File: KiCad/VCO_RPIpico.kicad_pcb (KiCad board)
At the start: 2 copper layers, 142 x 89 mm, 91 parts, among them J1 AudioJack2, J2 Power Jack, SW1 LFO1/2, SW2 Select LFO WaveForm, SW3 Fire4, SW4 Fire3, SW5 Fire2, SW6 Fire1, SW7 Shift2/Save, SW8 Shift1 / Select Bank, U2 PT2399, U3 L7805, sw10 sw_led_fire2, sw11 sw_led_fire3, sw12 sw_led_fire4, sw9 sw_led_fire1

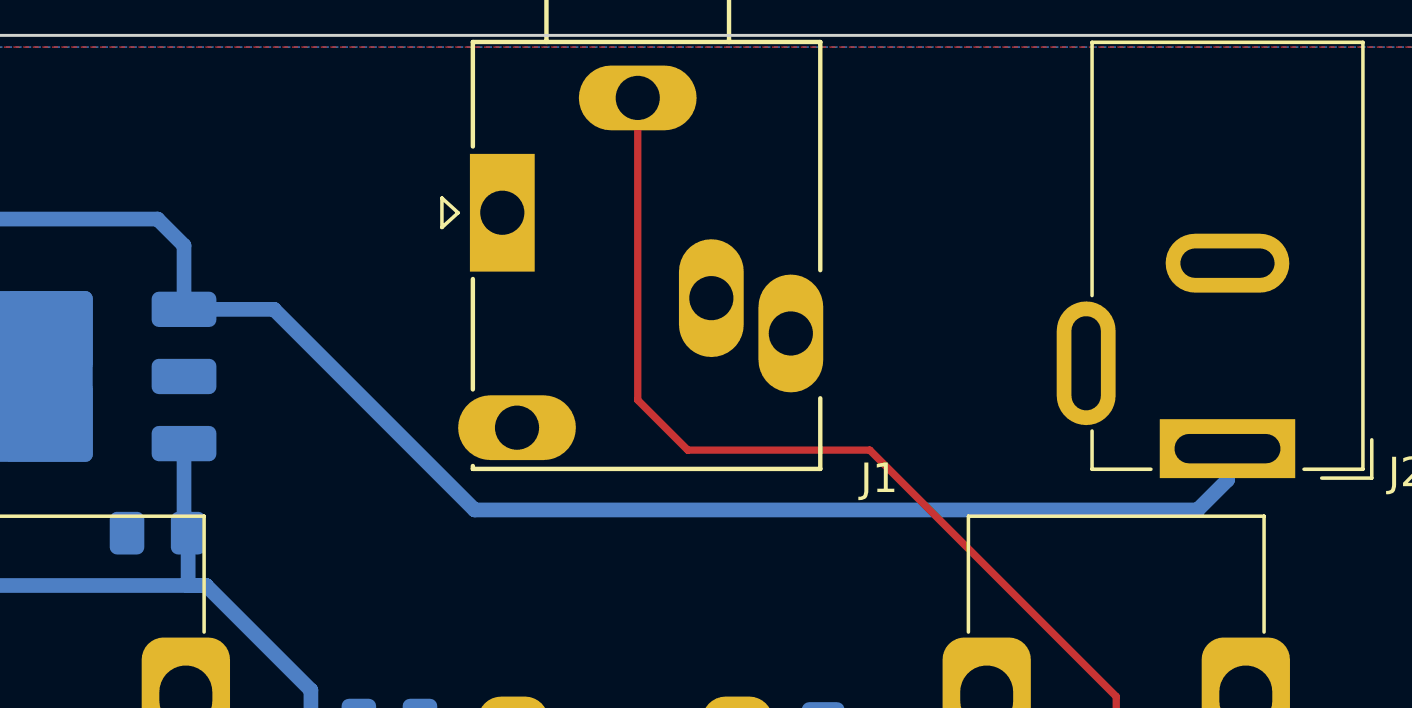
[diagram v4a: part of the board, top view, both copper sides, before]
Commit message: Kicad Schottkydiode added
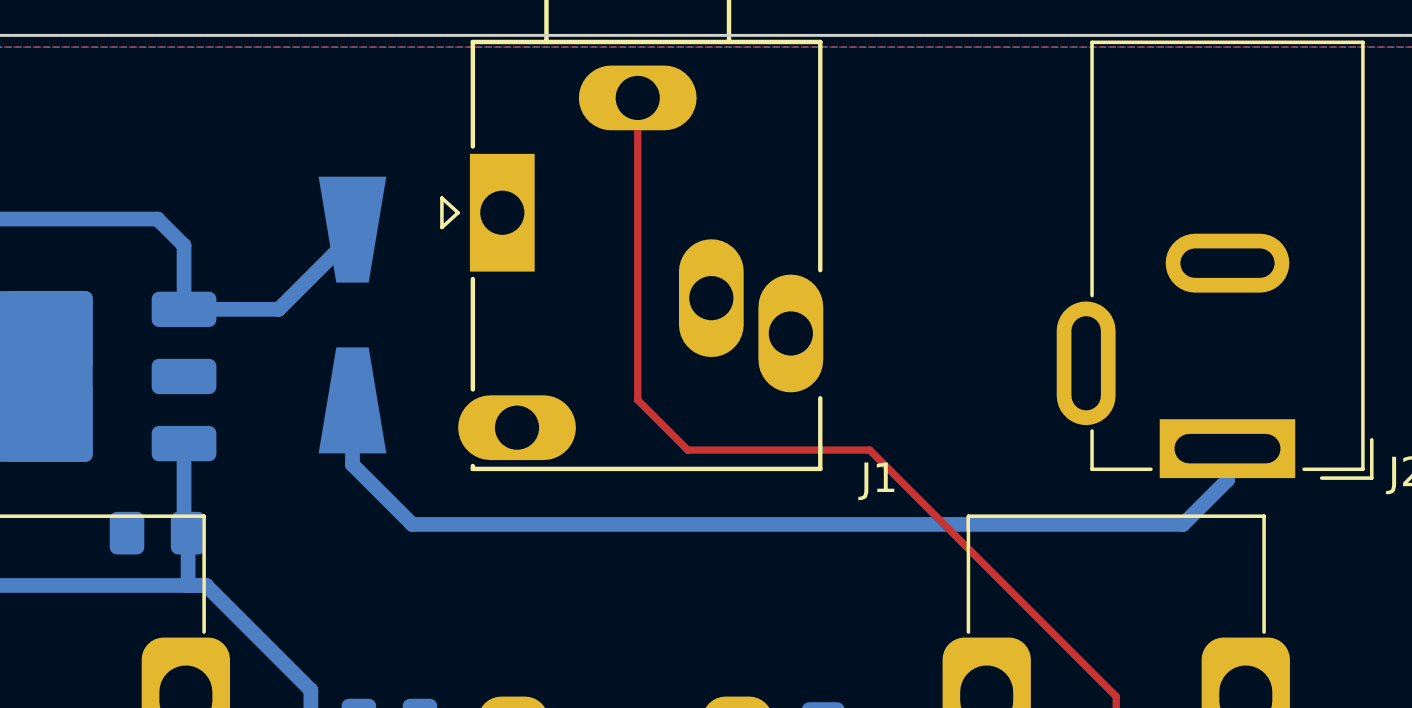
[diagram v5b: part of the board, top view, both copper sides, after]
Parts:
- added D20: SK110, Diode_SMD:D_SMA-SMB_Universal_Handsoldering, B.Cu at (139.1, 51.5)
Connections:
- C1 pad 1: Net-(U3-IN) -> Net-(D20-K)
- J2 pad 1: Net-(U3-IN) -> Net-(D20-A)
- U3 pad 1: Net-(U3-IN) -> Net-(D20-K)
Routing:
- net Net-(U3-IN): track 58.0 -> 0.00 mm
- net Net-(D20-A): track 0.00 -> 34.6 mm
- net Net-(D20-K): track 0.00 -> 25.0 mm

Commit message: Kicad kleine Änderung
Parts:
- J1: value AudioJack2 -> AudioJack
- RV5, RV6: value 50k -> 100k
- moved J2 52.0 mm to (117.2, 62.4)
- moved D20 26.5 mm to (117.2, 66.5), turned to 180 degrees
- moved C10 23.0 mm to (110.1, 53.5), turned to -90 degrees
- moved C1 20.1 mm to (139.3, 55.1), turned to 90 degrees
- moved J1 6.73 mm to (146.7, 54.3)
- moved U3 2.29 mm to (130.3, 54.8), turned to 0 degrees
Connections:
- R13 pad MP: (no net) -> GND
- R14 pad MP: (no net) -> GND
- R15 pad MP: (no net) -> GND
- RV4 pad MP: (no net) -> GND
- RV5 pad MP: (no net) -> GND
- RV6 pad MP: (no net) -> GND
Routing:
- net Net-(D20-A): track 34.6 -> 5.27 mm
- net +5C: track 130.6 -> 141.0 mm
- net Net-(J1-PadS): track 37.7 -> 28.6 mm
- net Net-(D20-K): track 25.0 -> 30.0 mm
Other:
- board size 142 x 89 mm -> 138 x 83 mm
- board text added: "Delay Time"
- board text added: "Echo Mix"
- board text added: "LFO Amount"
- board text added: "LFO Freq"
- board text added: "Tune"
- board text added: "Volume"

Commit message: Kicad Bezeichner hinzugefügt
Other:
- board text added: "DUB-IY DB4 rev.0 2024"
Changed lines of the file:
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@@
 		(tags "Diode Universal SMA (DO-214AC) SMB (DO-214AA) Handsoldering ")
 		(property "Reference" "D20"
-			(at 0 3 360)
+			(at 0 3 0)
 			(layer "B.SilkS")
 			(effects
@@
 		)
 		(property "Value" "SK110"
-			(at 0 -3.1 360)
+			(at 0 -3.1 0)
 			(layer "B.Fab")
 			(effects
@@
 		)
 		(fp_text user "${REFERENCE}"
-			(at 0 3 360)
+			(at 0 3 0)
 			(layer "B.Fab")
 			(effects
@@
 		(tags "DPAK TO-252 DPAK-3 TO-252-3 SOT-428")
 		(property "Reference" "U3"
-			(at 0.938 -4.547 360)
+			(at 0.938 -4.547 0)
 			(layer "B.SilkS")
 			(effects
@@
 		)
 		(property "Value" "L7805"
-			(at 0.176 -2.0195 360)
+			(at 0.176 -2.0195 0)
 			(layer "B.Fab")
 			(effects
@@
 		)
 		(fp_text user "${REFERENCE}"
-			(at 0 0 360)
+			(at 0 0 0)
 			(layer "B.Fab")
 			(effects
@@
 		)
 	)
+	(gr_rect
+		(start 136.35 107.7)
+		(end 159.05 113.3)
+		(stroke
+			(width 0.15)
+			(type default)
+		)
+		(fill none)
+		(layer "B.SilkS")
+	)
 	(gr_circle
 		(center 177 51)
@@
 		(layer "User.1")
 	)
+	(gr_text "DUB-IY DB4 rev.0\n2024"
+		(at 158.1 112.7 0)
+		(layer "B.SilkS")
+		(effects
+			(font
+				(size 1.5 1.5)
+				(thickness 0.3)
+				(bold yes)
+			)
+			(justify left bottom mirror)
+		)
+	)
 	(gr_text "Tune"
